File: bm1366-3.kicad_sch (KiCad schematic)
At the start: 52 parts, among them U14 BM1366_mode1, U23 ADP171AUJ-R7, U24 ADP171AUJ-R7

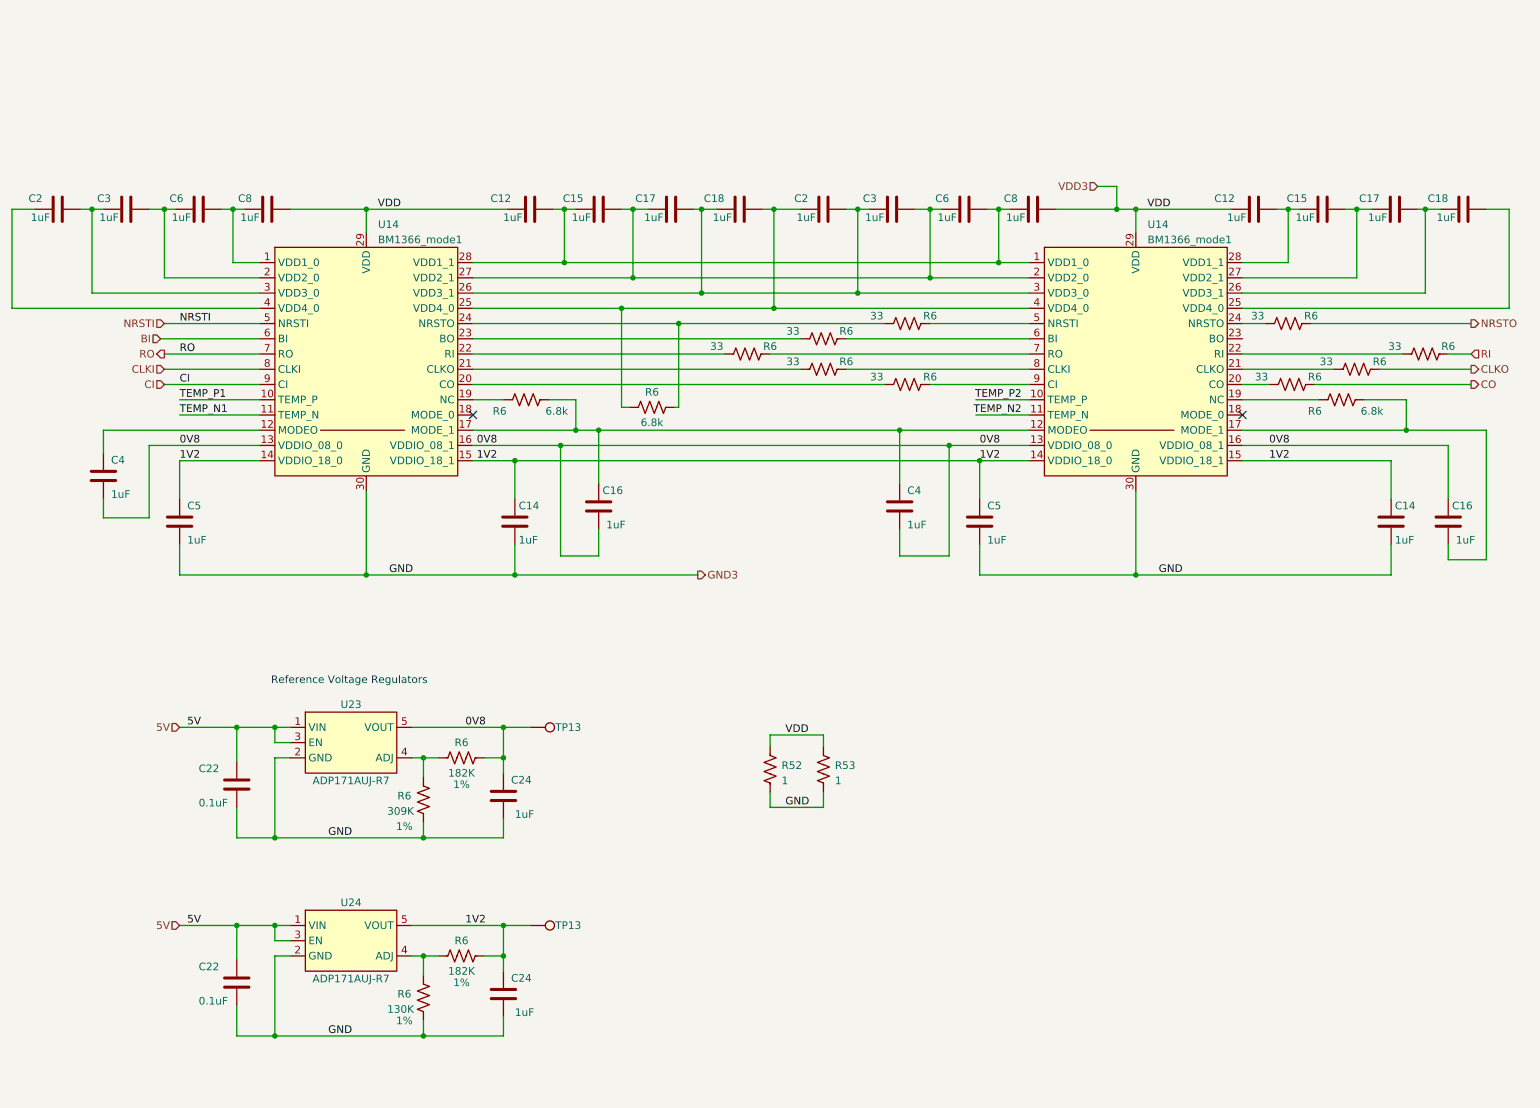
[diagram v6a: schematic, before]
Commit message: add level translator circuits to ASIC communications
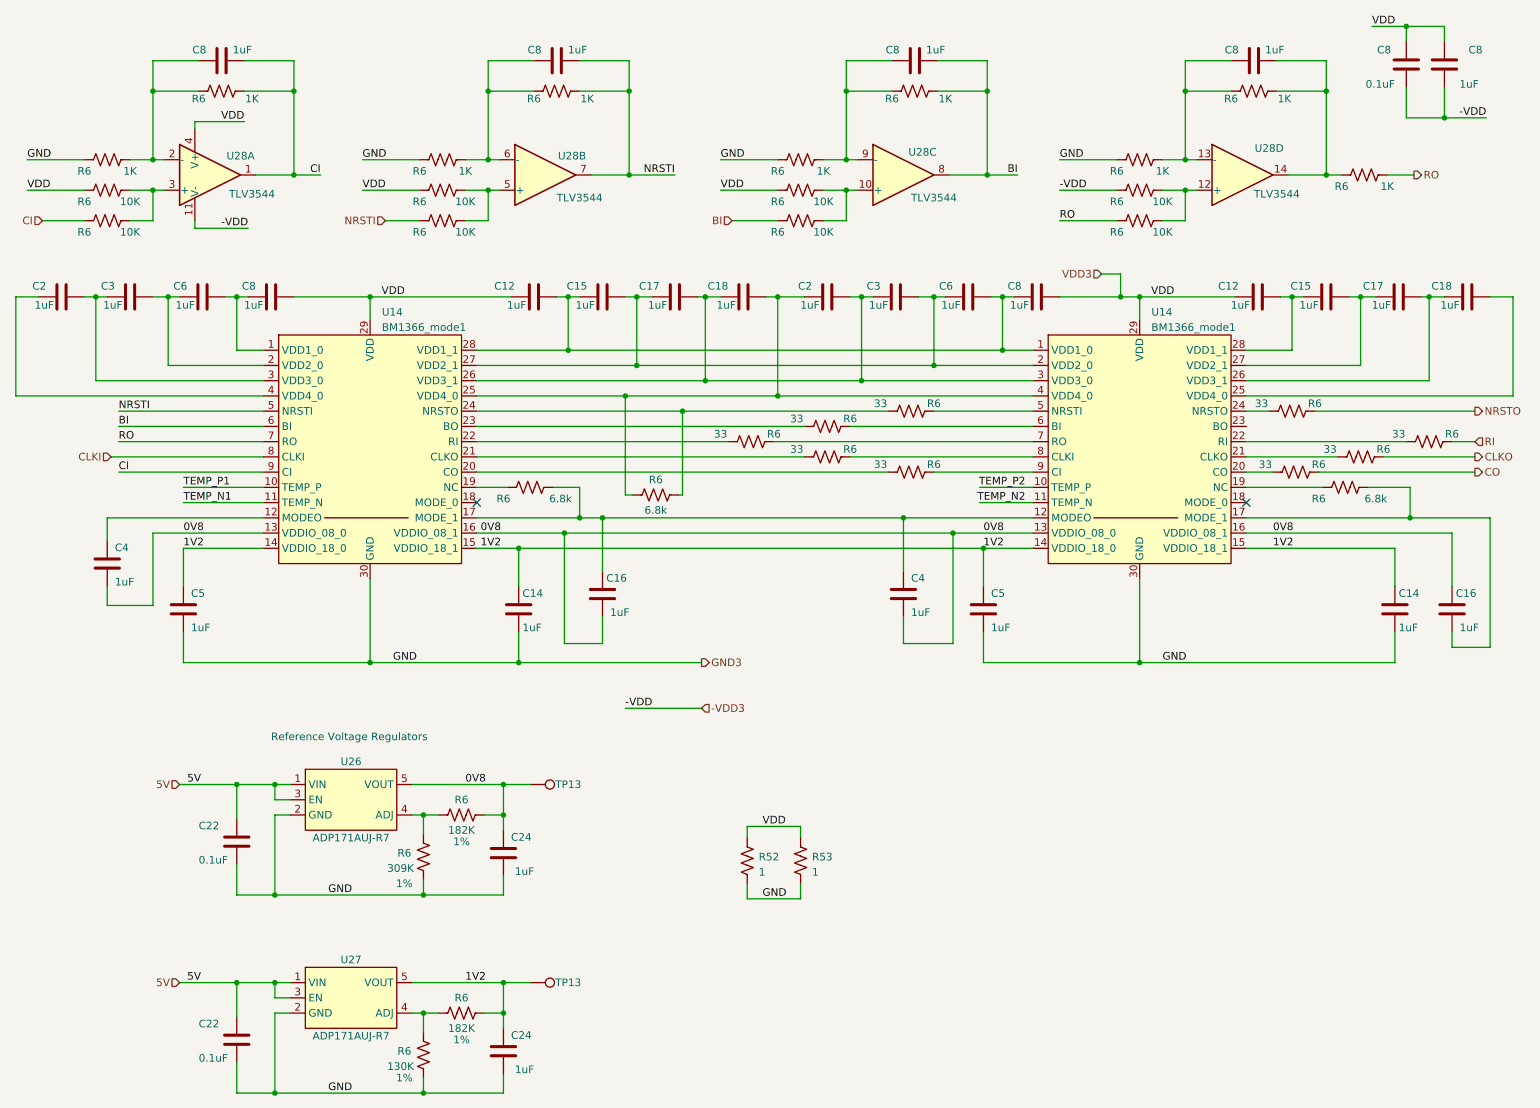
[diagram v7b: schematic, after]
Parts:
- added C8: 0.1uF, Capacitor_SMD:C_0402_1005Metric, symbol Device:C
- added C8 (x5): 1uF, Capacitor_SMD:C_0402_1005Metric, symbol Device:C
- added R6 (x9): 1K, Resistor_SMD:R_0402_1005Metric, symbol Device:R_US
- added R6 (x8): 10K, Resistor_SMD:R_0402_1005Metric, symbol Device:R_US
- added U28: TLV3544, Package_SO:TSSOP-14_4.4x5mm_P0.65mm, symbol bitaxe:TLV3544
- renumbered U23 to U26, U24 to U27
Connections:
- net BI: now also C8.2, R6.1, R6.1, U28.8
- net CI: now also C8.2, R6.1, R6.1, U28.1
- net GND3: now also R6.2, R6.2, R6.2, R6.2
- net NRSTI: now also C8.2, R6.1, R6.1, U28.7
- net RO: now also R6.1, R6.1
- net VDD3: now also C8.2, C8.2, R6.1, R6.1, R6.1, U28.4 (V+)
- new net: C8.1, R6.1, R6.2, U28.13 (-)
- new net: R6.2, R6.2, U28.5 (+)
- new net: C8.1, R6.1, R6.2, U28.6 (-)
- new net: C8.1, R6.1, R6.2, U28.9 (-)
- new net: C8.2, R6.1, R6.2, U28.14
- new net: R6.2, R6.2, U28.10 (+)
- new net: C8.1, R6.1, R6.2, U28.2 (-)
- new net: R6.2, R6.2, U28.12 (+)
- new net: R6.2, R6.2, U28.3 (+)
- new net -VDD3: C8.1, C8.1, R6.1, U28.11 (V-)
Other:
- moved on the sheet: C12, C14, C15, C16, C17, C18, C2, C22, C24, C3, C4, C5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

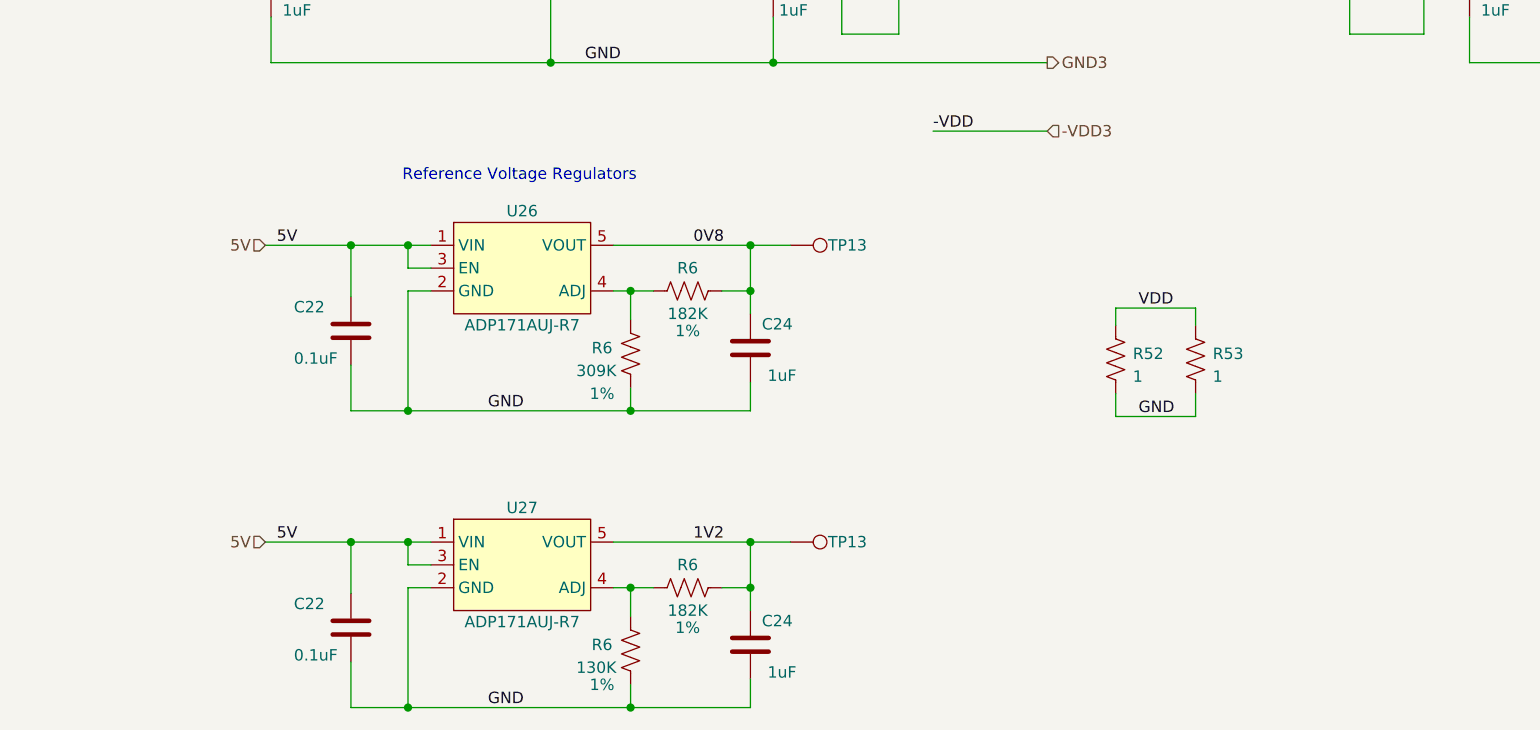
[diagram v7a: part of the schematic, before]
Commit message: Update temperature sensors, start deep review
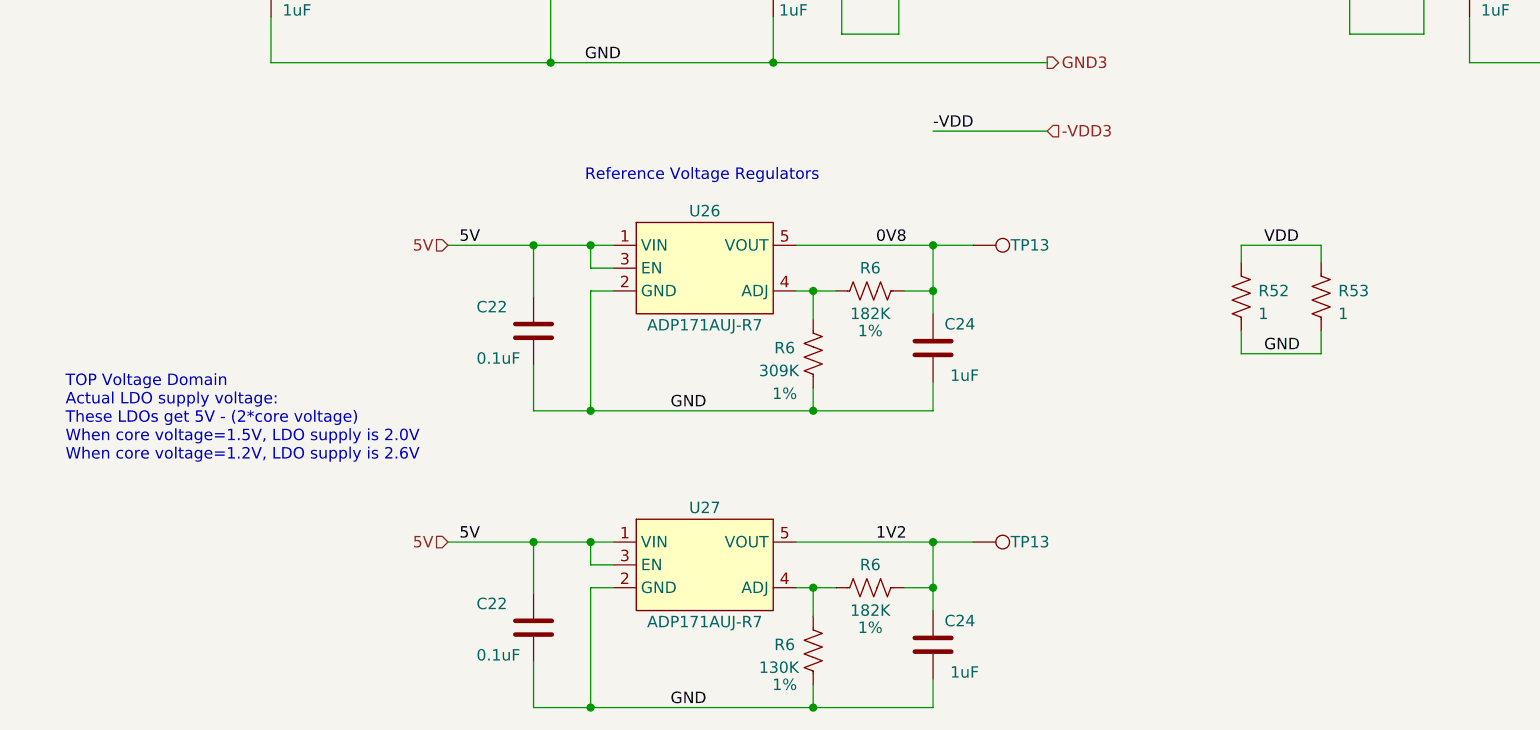
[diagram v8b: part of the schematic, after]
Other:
- note added: "TOP Voltage Domain Actual LDO supply voltage: These LDOs get 5V - (2*core voltage) When core voltage=1.5V, LDO supply is 2.0V When core voltage=1.2V, LDO supply is 2.6V"
- moved on the sheet: C22, C24, R52, R53, R6, TP13, U26, U27
